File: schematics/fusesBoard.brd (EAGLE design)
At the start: 76 x 76 mm, 0 parts

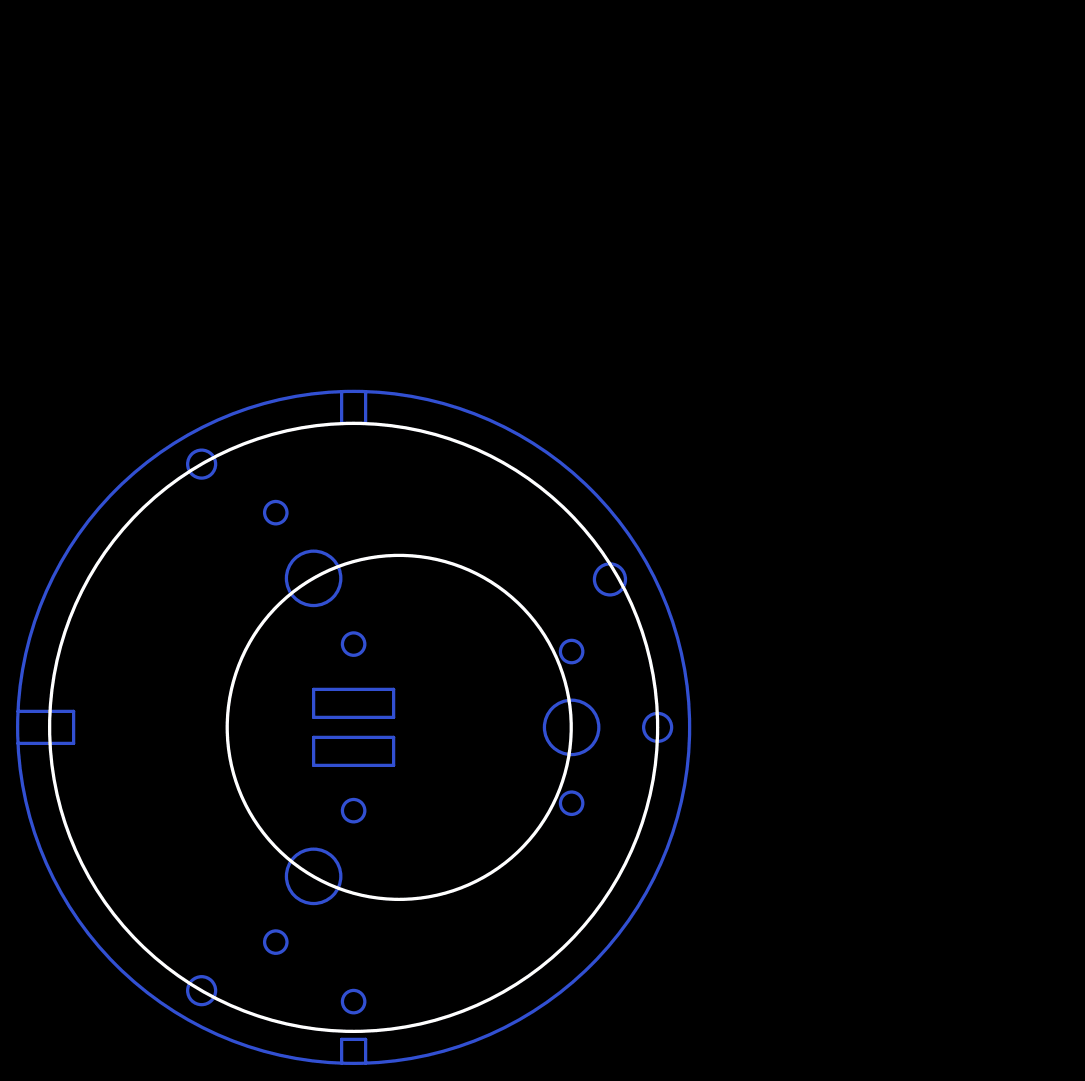
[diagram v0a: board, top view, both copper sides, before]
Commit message: готова схема платы с пережигателями
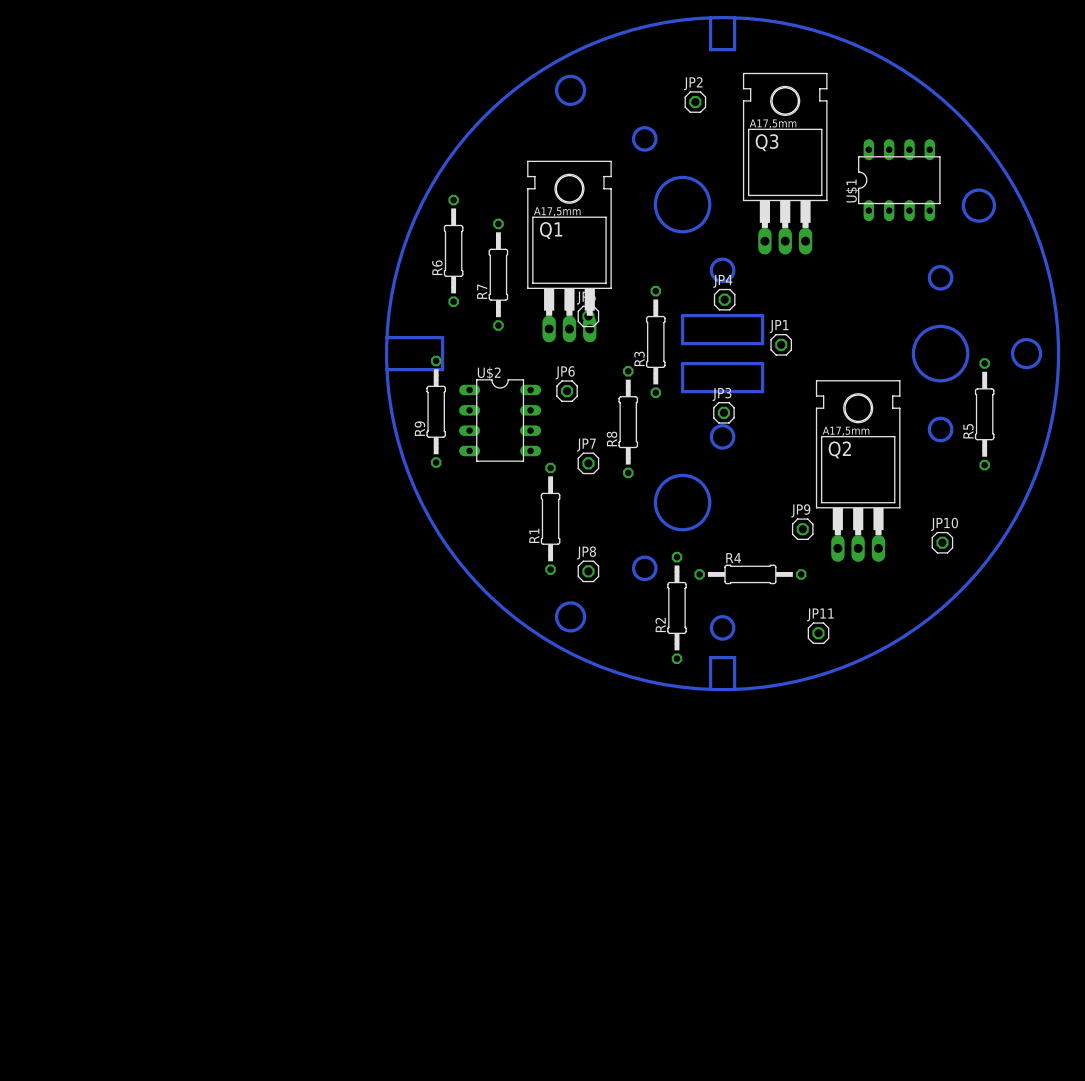
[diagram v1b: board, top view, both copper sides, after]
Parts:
- added JP1, JP10, JP11, JP2, JP3, JP4, JP5, JP6, JP7, JP8, JP9: (no value), pinhead:1X01
- added Q1, Q2, Q3: IRF540, transistor-fet:TO220
- added R1, R2, R3: (no value), rcl:0207/12
- added R4, R6, R8: 1k, rcl:0207/12
- added R5, R7, R9: 10k, rcl:0207/12
- added U$1, U$2: KP249KH5, optron1:DIL08
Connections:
- new net +7V: JP4.1, JP7.1, JP9.1, R4.2, R6.2, R8.1
- new net GND: Q1.3, Q2.3, Q3.3, R1.1, R2.1, R3.2, R5.1, R7.1, R9.1
- new net N$10: Q2.1, R5.2, U$1.8
- new net N$11: R4.1, U$1.7
- new net N$12: Q1.1, R7.2, U$2.8
- new net N$13: JP1.1, U$1.1
- new net N$14: JP3.1, Q2.2
- new net N$15: R6.1, U$2.7
- new net N$16: JP5.1, U$2.1
- new net N$17: R2.2, U$1.2
- new net N$18: R1.2, U$2.2
- new net N$19: JP6.1, Q1.2
- new net N$20: Q3.1, R9.2, U$1.5
- new net N$22: R8.2, U$1.6
- new net N$23: JP8.1, Q3.2
- new net N$25: JP2.1, U$1.4
- new net N$26: R3.1, U$1.3
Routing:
- net N$7: track 19.8 -> 21.8 mm
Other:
- board outline removed

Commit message: разведена плата для пережигателей
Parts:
- removed JP10, JP11: (no value), pinhead:1X01
- added JP13, JP14, JP15: (no value), pinhead:1X01
- R1: value (none) -> 10k; device rcl:0207/12 -> resistor:0204/7
- R2, R7, R8: device rcl:0207/12 -> resistor:0204/7
- R3: value (none) -> 1k; device rcl:0207/12 -> resistor:0204/7
- R4: value 1k -> (none); device rcl:0207/12 -> resistor:0204/7
- R5: value 10k -> 1k; device rcl:0207/12 -> resistor:0204/7
- R6: value 1k -> 10k; device rcl:0207/12 -> resistor:0204/7
- R9: value 10k -> (none); device rcl:0207/12 -> resistor:0204/7
- moved R5 64.6 mm to (14.3, 38.7), turned to 270 degrees
- moved R9 64.6 mm to (72.4, 21.7), turned to 270 degrees
- moved JP5 57.4 mm to (71.0, 11.8)
- moved R7 54.2 mm to (49.4, 12.3), turned to 0 degrees
- moved R1 51.9 mm to (47.1, 72.8), turned to 0 degrees
- moved R4 50.1 mm to (12.9, 53.3)
- moved R2 49.3 mm to (12.9, 55.9), turned to 0 degrees
- moved Q3 49.3 mm to (26.1, 26.5), turned to 180 degrees
- moved U$2 47.1 mm to (61.4, 19.1), turned to 90 degrees
- moved U$1 46.5 mm to (24.9, 51.6), turned to 270 degrees
- moved JP2 45.6 mm to (8.70, 47.8)
- moved JP9 42.1 mm to (14.4, 30.2)
- moved JP1 41.6 mm to (14.7, 62.7)
- moved Q2 35.3 mm to (57.2, 63.5), turned to 270 degrees
- moved Q1 33.4 mm to (58.7, 45.6), turned to 180 degrees
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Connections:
- removed net +7V: JP4.1, JP7.1, JP9.1, R4.2, R6.2, R8.1
- new net VCC1: JP13.1, JP7.1, R8.2
- new net VCC2: JP14.1, JP4.1, R3.2
- new net VCC3: JP15.1, JP9.1, R5.2
- net GND: now also R4.1, R6.1; no longer R3.2, R5.1
- net N$10: now also R1.2; no longer R5.2
- net N$11: now also R3.1; no longer R4.1
- net N$15: now also R8.1; no longer R6.1
- net N$18: now also R9.2; no longer R1.2
- net N$20: now also R6.2; no longer R9.2
- net N$22: now also R5.1; no longer R8.2
- net N$26: now also R4.2; no longer R3.1
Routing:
- net N$12: track 0.00 -> 50.0 mm
- net VCC1: track 0.00 -> 44.8 mm
- net VCC2: track 0.00 -> 38.4 mm
- net N$10: track 0.00 -> 33.4 mm
- net N$23: track 0.00 -> 28.5 mm
- net N$1: track 0.00 -> 24.3 mm
- net N$7: track 21.8 -> 0.00 mm
- net N$22: track 0.00 -> 21.0 mm
- net N$20: track 0.00 -> 20.8 mm
- net N$9: track 13.9 -> 0.00 mm
- net N$5: track 13.5 -> 0.00 mm
- net N$2 (its old number): track 13.5 -> 0.00 mm
- net N$25: track 0.00 -> 12.4 mm
- net VCC3: track 0.00 -> 10.7 mm
- net N$4: track 10.0 -> 0.00 mm
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- added copper zone on layer 1, net GND
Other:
- board outline added: 84 x 84 mm
- board text added: "by GRANUM"
- board text added: "made on Earth"

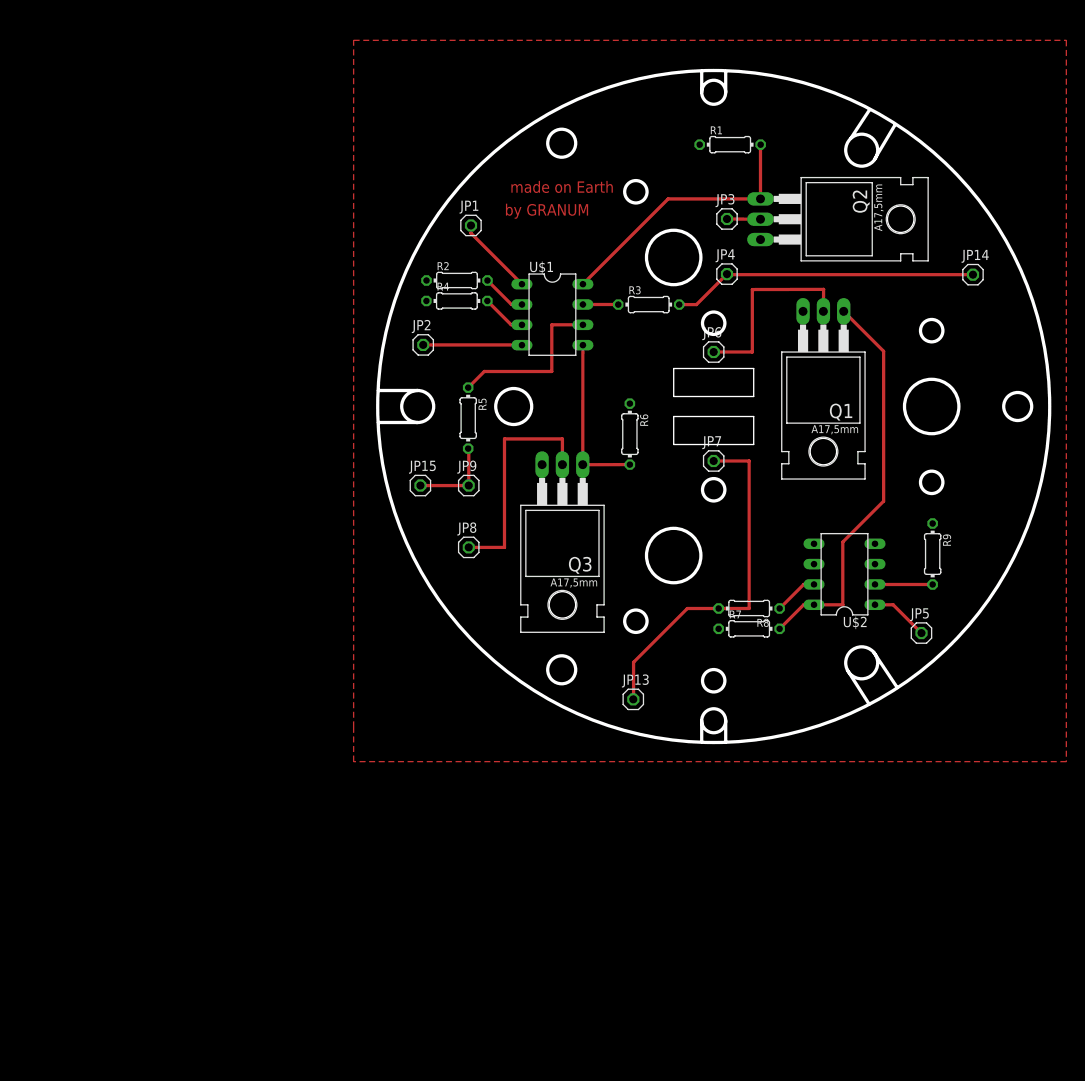
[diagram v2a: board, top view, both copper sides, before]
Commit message: сделаны площадки под пережигатели, увеличена ширина дорожек
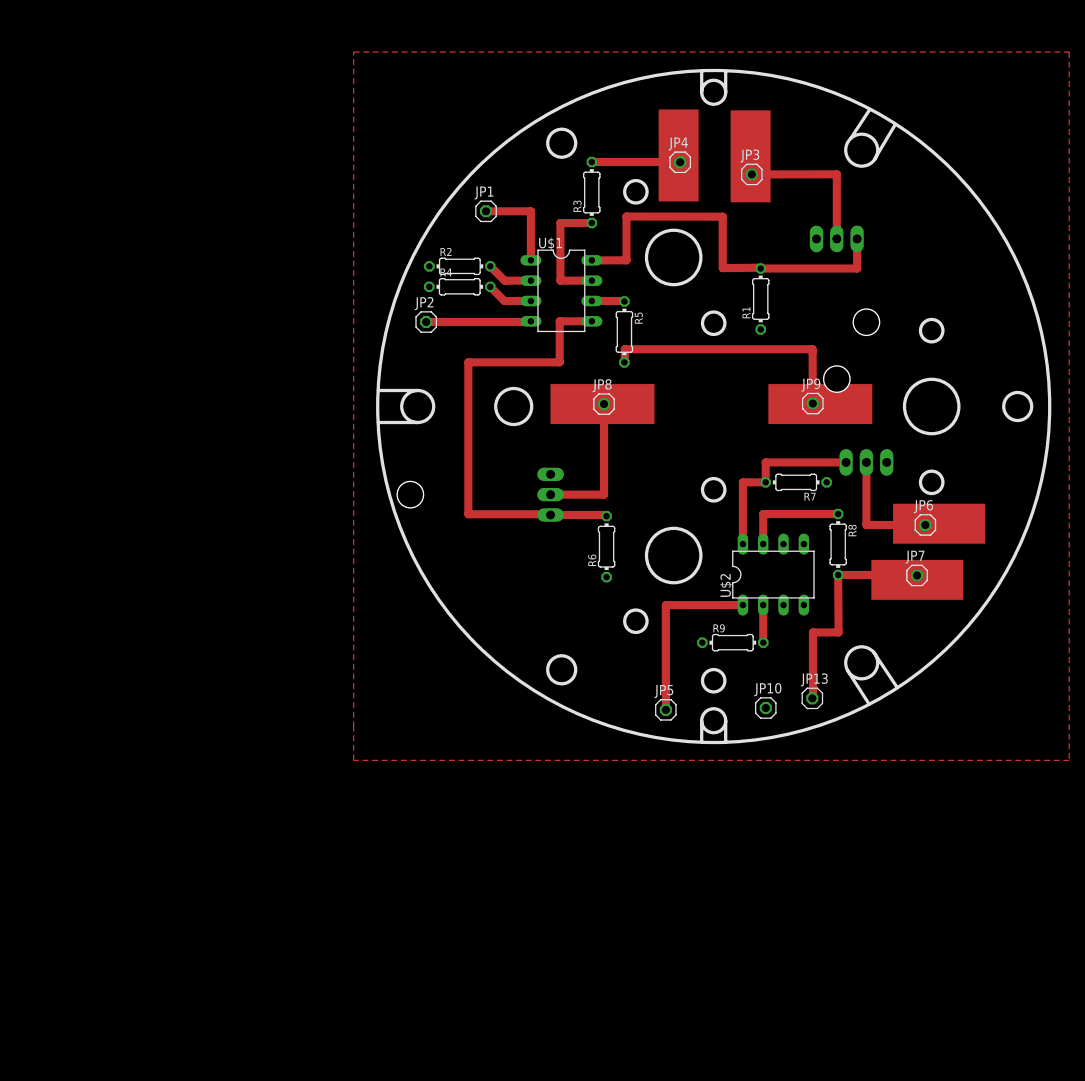
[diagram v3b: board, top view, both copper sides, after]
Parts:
- removed JP14, JP15: (no value), pinhead:1X01
- removed Q1, Q2, Q3: IRF540, transistor-fet:TO220
- added JP10: (no value), pinhead:1X01
- added U$3, U$4, U$5: IRF540, optron1:TO220
- moved JP9 44.2 mm to (57.4, 40.5)
- moved JP6 34.2 mm to (71.5, 25.3)
- moved JP5 33.4 mm to (39.0, 2.19)
- moved JP7 29.2 mm to (70.4, 19.0)
- moved R9 27.3 mm to (47.4, 10.6), turned to 0 degrees
- moved JP8 24.6 mm to (31.3, 40.4)
- moved JP13 22.4 mm to (57.3, 3.63)
- moved R5 22.3 mm to (33.9, 49.4)
- moved R1 19.7 mm to (50.9, 53.5), turned to 90 degrees
- moved R7 19.2 mm to (55.3, 30.6), turned to 180 degrees
- moved R3 15.7 mm to (29.8, 66.9), turned to 90 degrees
- moved JP4 15.2 mm to (40.8, 70.6)
- moved R6 14.4 mm to (31.6, 22.6), turned to 90 degrees
- moved R8 13.7 mm to (60.6, 22.9), turned to 270 degrees
- moved U$2 8.89 mm to (52.5, 19.1), turned to 0 degrees
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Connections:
- removed net VCC1: JP13.1, JP7.1, R8.2
- removed net VCC2: JP14.1, JP4.1, R3.2
- removed net VCC3: JP15.1, JP9.1, R5.2
- new net VCC: JP13.1, JP4.1, JP7.1, JP9.1, R3.2, R5.2, R8.2
- net GND: now also JP10.1, U$3.SOURCE, U$4.SOURCE, U$5.SOURCE; no longer Q1.3, Q2.3, Q3.3
- net N$1: now also U$5.DRAIN; no longer Q1.2
- net N$10: now also U$3.GATE; no longer Q2.1
- net N$12: now also U$5.GATE; no longer Q1.1
- net N$14: now also U$3.DRAIN; no longer Q2.2
- net N$20: now also U$4.GATE; no longer Q3.1
- net N$23: now also U$4.DRAIN; no longer Q3.2
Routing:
- net VCC: track 0.00 -> 71.7 mm
- net VCC1: track 44.8 -> 0.00 mm
- net VCC2: track 38.4 -> 0.00 mm
- net N$20: track 20.8 -> 57.1 mm
- net N$12: track 50.0 -> 23.1 mm
- net N$22: track 21.0 -> 4.13 mm
- net N$10: track 33.4 -> 48.9 mm
- net N$2: track 7.28 -> 22.7 mm
- net N$14: track 4.19 -> 18.7 mm
- net VCC3: track 10.7 -> 0.00 mm
- net N$11: track 4.43 -> 15.1 mm
- net N$23: track 28.5 -> 18.0 mm
- net N$1: track 24.3 -> 15.2 mm
- net N$15: track 5.55 -> 13.1 mm
- net N$18: track 7.22 -> 4.70 mm
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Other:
- board outline removed
- board text removed: "by GRANUM"
- board text removed: "made on Earth"

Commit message: переразведенная схема платы
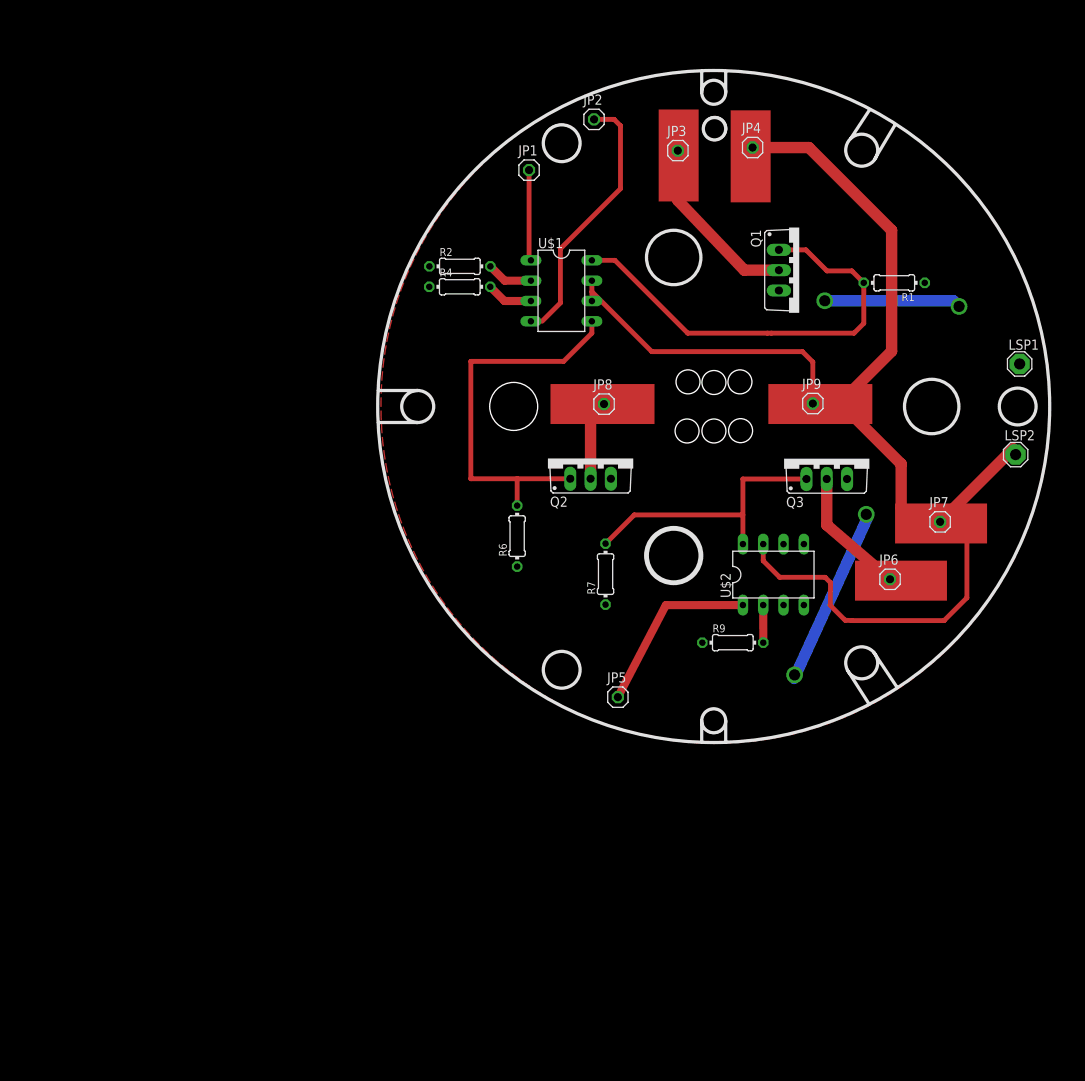
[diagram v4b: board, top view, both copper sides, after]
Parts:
- removed JP10, JP13: (no value), pinhead:1X01
- removed R3, R5, R8: 1k, resistor:0204/7
- removed U$3, U$4, U$5: IRF540, optron1:TO220
- added LSP1, LSP2: SE14, solpad:SE14
- added Q1, Q2, Q3: IRF540, transistor-power:TO220BV
- R1, R6, R7: value 10k -> 10000
- R2, R4, R9: value (none) -> 50
- moved JP2 32.9 mm to (30.1, 76.0)
- moved R7 26.4 mm to (31.5, 19.2), turned to 90 degrees
- moved R1 16.8 mm to (67.6, 55.6), turned to 180 degrees
- moved R6 11.3 mm to (20.4, 23.9)
- moved JP3 9.72 mm to (40.5, 72.1)
- moved JP4 9.24 mm to (49.9, 72.5)
- moved JP6 8.10 mm to (67.0, 18.5)
- moved JP1 7.45 mm to (21.9, 69.7)
- moved JP7 7.29 mm to (73.3, 25.7)
- moved JP5 6.21 mm to (33.0, 3.78)
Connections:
- net N$13 renamed CTRL1
- net N$2 renamed CTRL3
- net N$25 renamed CTRL2
- removed net N$1: JP6.1, U$5.DRAIN
- removed net N$10: R1.2, U$1.8, U$3.GATE
- removed net N$11: R3.1, U$1.7
- removed net N$12: R7.2, U$2.8, U$5.GATE
- removed net N$14: JP3.1, U$3.DRAIN
- removed net N$15: R8.1, U$2.7
- removed net N$20: R6.2, U$1.5, U$4.GATE
- removed net N$22: R5.1, U$1.6
- removed net N$23: JP8.1, U$4.DRAIN
- new net GATE1: Q1.G, R1.2, U$1.8
- new net GATE2: Q2.G, R6.2, U$1.5
- new net GATE3: Q3.G, R7.2, U$2.8
- new net SOURCE1: JP3.1, Q1.D
- new net SOURCE2: JP8.1, Q2.D
- new net SOURCE3: JP6.1, Q3.D
- net GND: now also LSP1.MP, Q1.S, Q2.S, Q3.S; no longer JP10.1, U$3.SOURCE, U$4.SOURCE, U$5.SOURCE
- net VCC: now also LSP2.MP, U$1.6, U$1.7, U$2.7; no longer JP13.1, R3.2, R5.2, R8.2
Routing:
- net VCC: track 71.7 -> 175.2 mm
- net N$20: track 57.1 -> 0.00 mm
- net GATE1: track 0.00 -> 55.7 mm
- net N$10: track 48.9 -> 0.00 mm
- net GATE2: track 0.00 -> 48.5 mm
- net GATE3: track 0.00 -> 38.4 mm
- net N$12: track 23.1 -> 0.00 mm
- net SOURCE1: track 0.00 -> 22.6 mm
- net CTRL2: track 13.1 -> 33.5 mm
- net N$14: track 18.7 -> 0.00 mm
- net N$23: track 18.0 -> 0.00 mm
- net GND: track 0.00 -> 17.1 mm, vias 0 -> 4
- net SOURCE3: track 0.00 -> 16.2 mm
- net N$11: track 15.1 -> 0.00 mm
- net N$15: track 13.1 -> 0.00 mm
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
